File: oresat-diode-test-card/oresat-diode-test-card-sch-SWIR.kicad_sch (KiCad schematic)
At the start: 19 parts, among them Q3 NMOS, Q4 DMP3050LVT-7, U4 TLV6001DCK, U8 NX3L4051-Q100, U9 TLV6001DCK

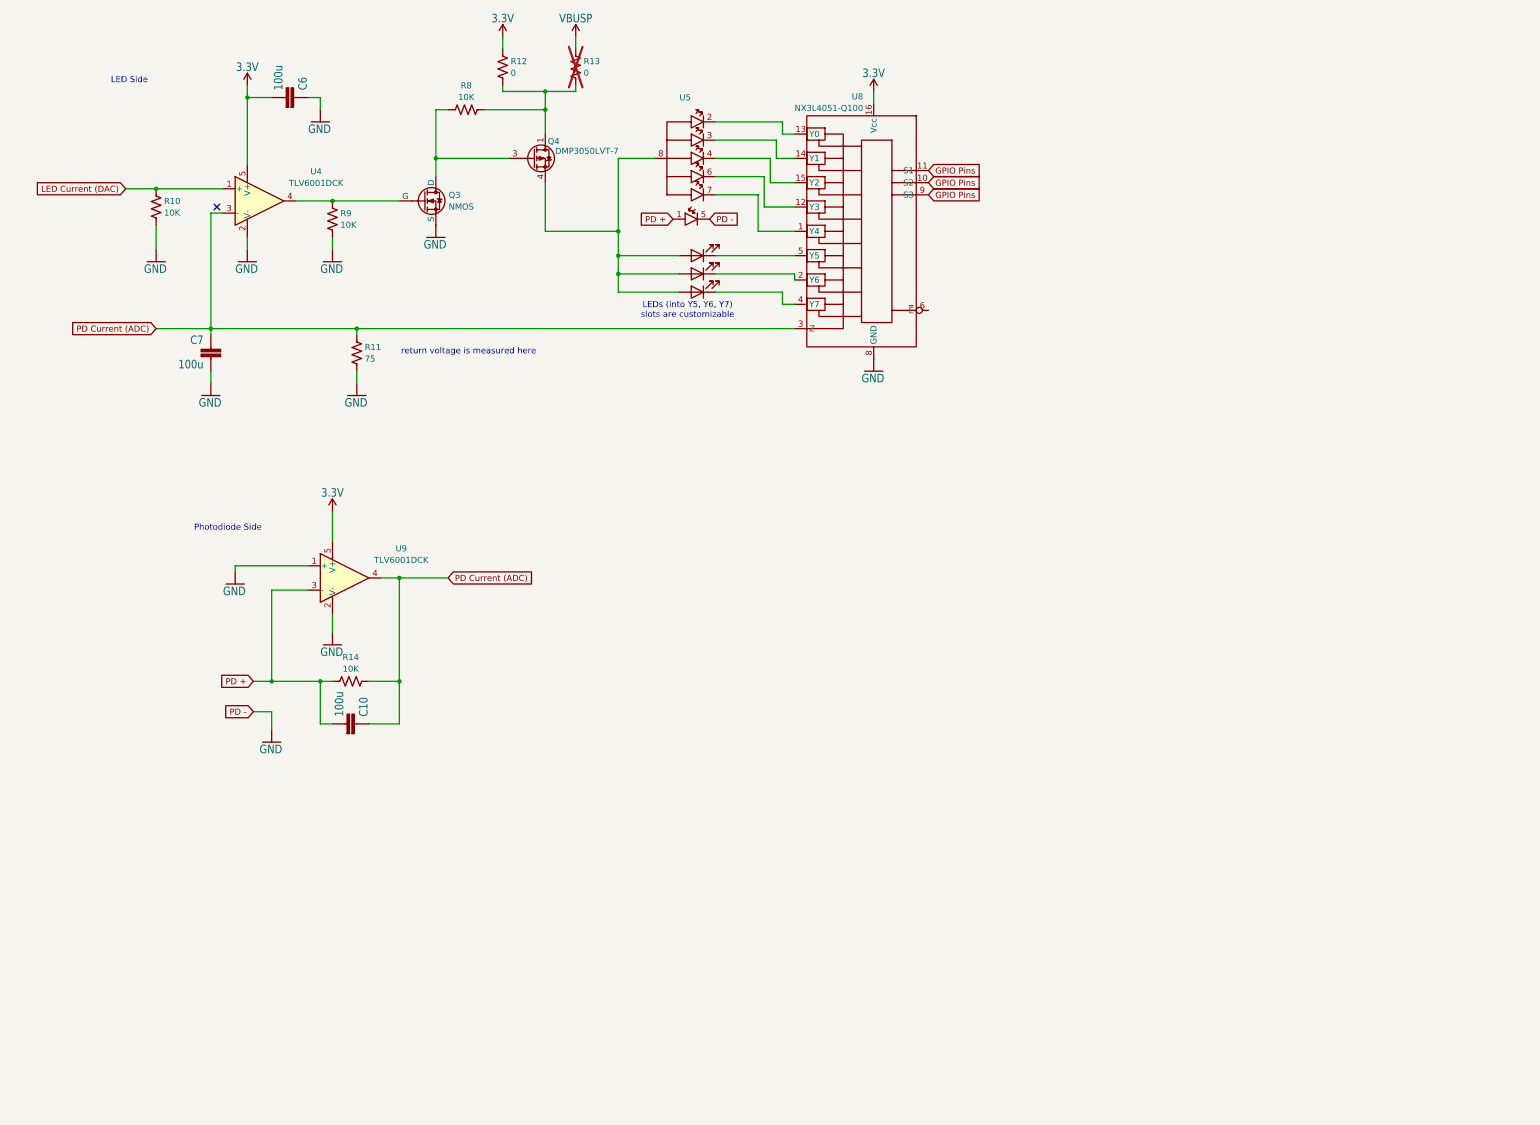
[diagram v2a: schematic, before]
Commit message: Quick design review on schematic; basically ready for layout.
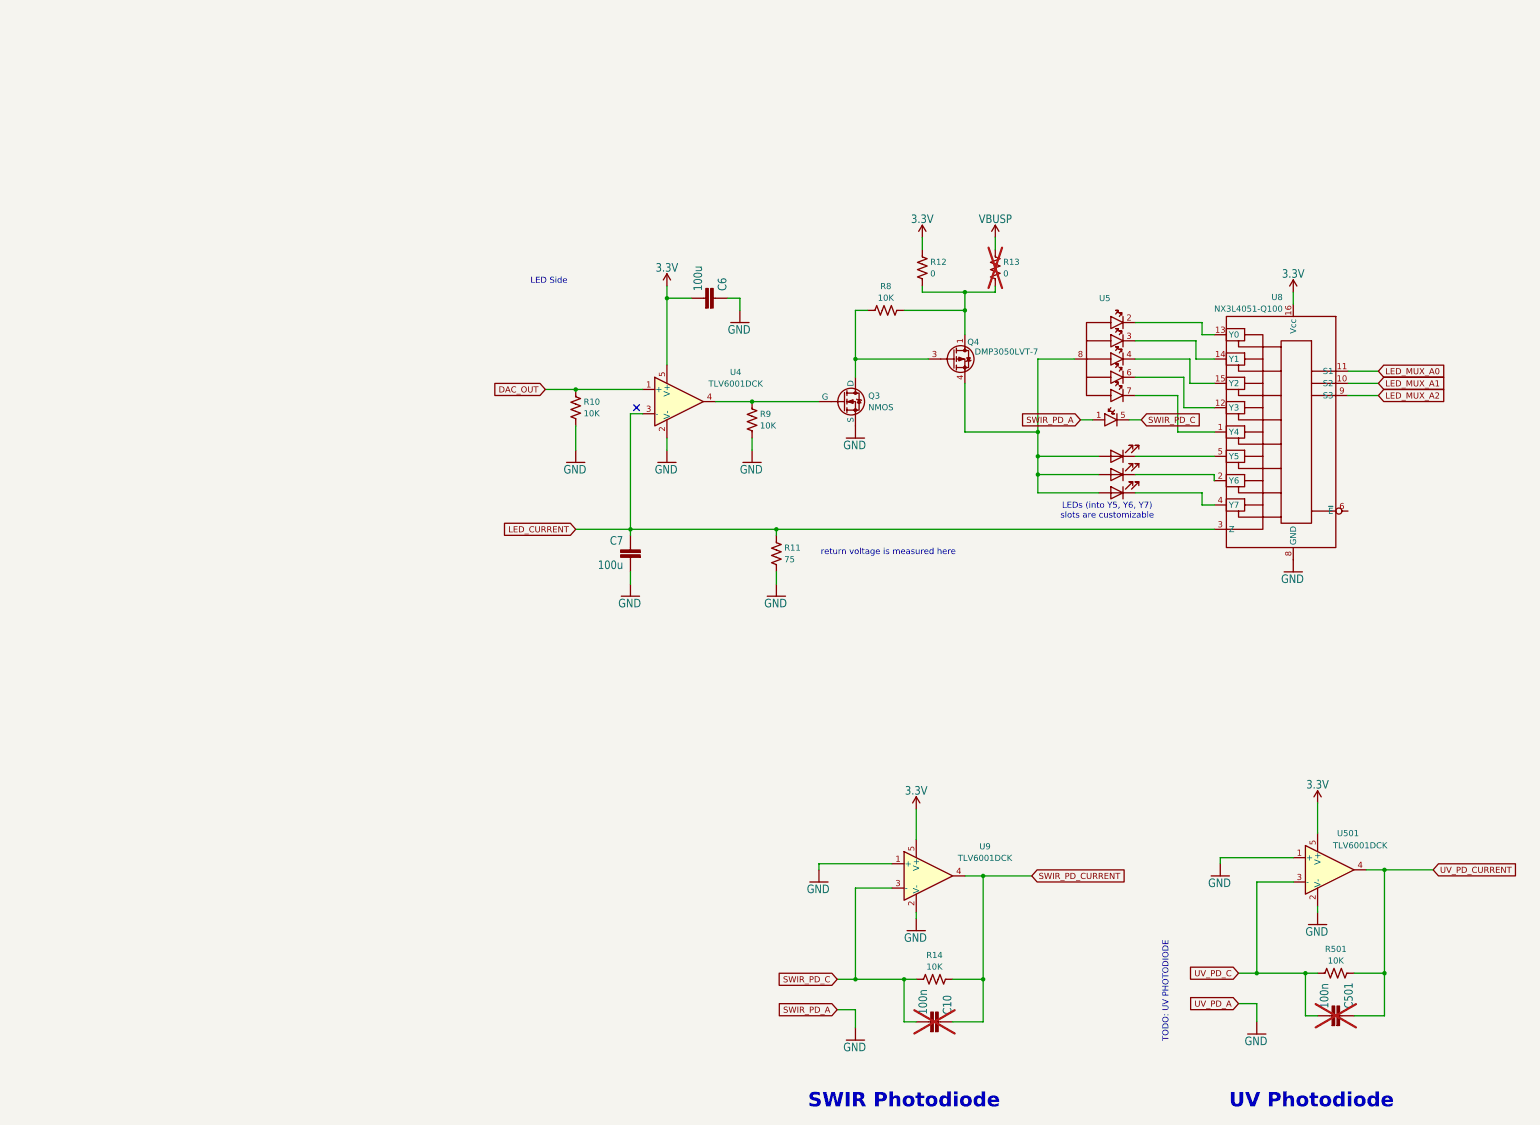
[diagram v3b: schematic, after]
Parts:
- added C501: 100n, oresat-passives:0603-C-NOSILK, symbol oresat-proto-card-eagle-import:C-EU0603-C-NOSILK
- added R501: 10K, symbol Device:R_US
- added U501: TLV6001DCK, Package_TO_SOT_SMD:SOT-353_SC-70-5, symbol Amplifier_Operational:TLV6001DCK
- C10: value 100u -> 100n; now not fitted; now left out of the parts list
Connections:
- net 3.3V: now also U501.5 (V+)
- net GND: now also U5.1 (PD_Anode), U501.1 (+), U501.2 (V-); no longer U5.5 (PD_Cathode)
- removed net GPIO Pins: U8.10 (S2), U8.11 (S1), U8.9 (S3)
- net LED Current (DAC) renamed DAC_OUT
- net PD + renamed SWIR_PD_C
- net SWIR_PD_C: now also U5.5 (PD_Cathode); no longer U5.1 (PD_Anode)
- net PD Current (ADC) renamed LED_CURRENT
- net LED_CURRENT: no longer C10.1, R14.2, U9.4
- new net LED_MUX_A0: U8.11 (S1)
- new net LED_MUX_A1: U8.10 (S2)
- new net LED_MUX_A2: U8.9 (S3)
- new net SWIR_PD_CURRENT: C10.1, R14.2, U9.4
- new net UV_PD_C: C501.2, R501.1, U501.3 (-)
- new net UV_PD_CURRENT: C501.1, R501.2, U501.4
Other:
- note added: "SWIR Photodiode"
- note added: "TODO: UV PHOTODIODE"
- note added: "UV Photodiode"
- note removed: "Photodiode Side"
- title: (none) -> OreSat Diode Test Card
- moved on the sheet: C6, C7, Q3, Q4, R10, R11, R12, R13, R14, R8, R9, U4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

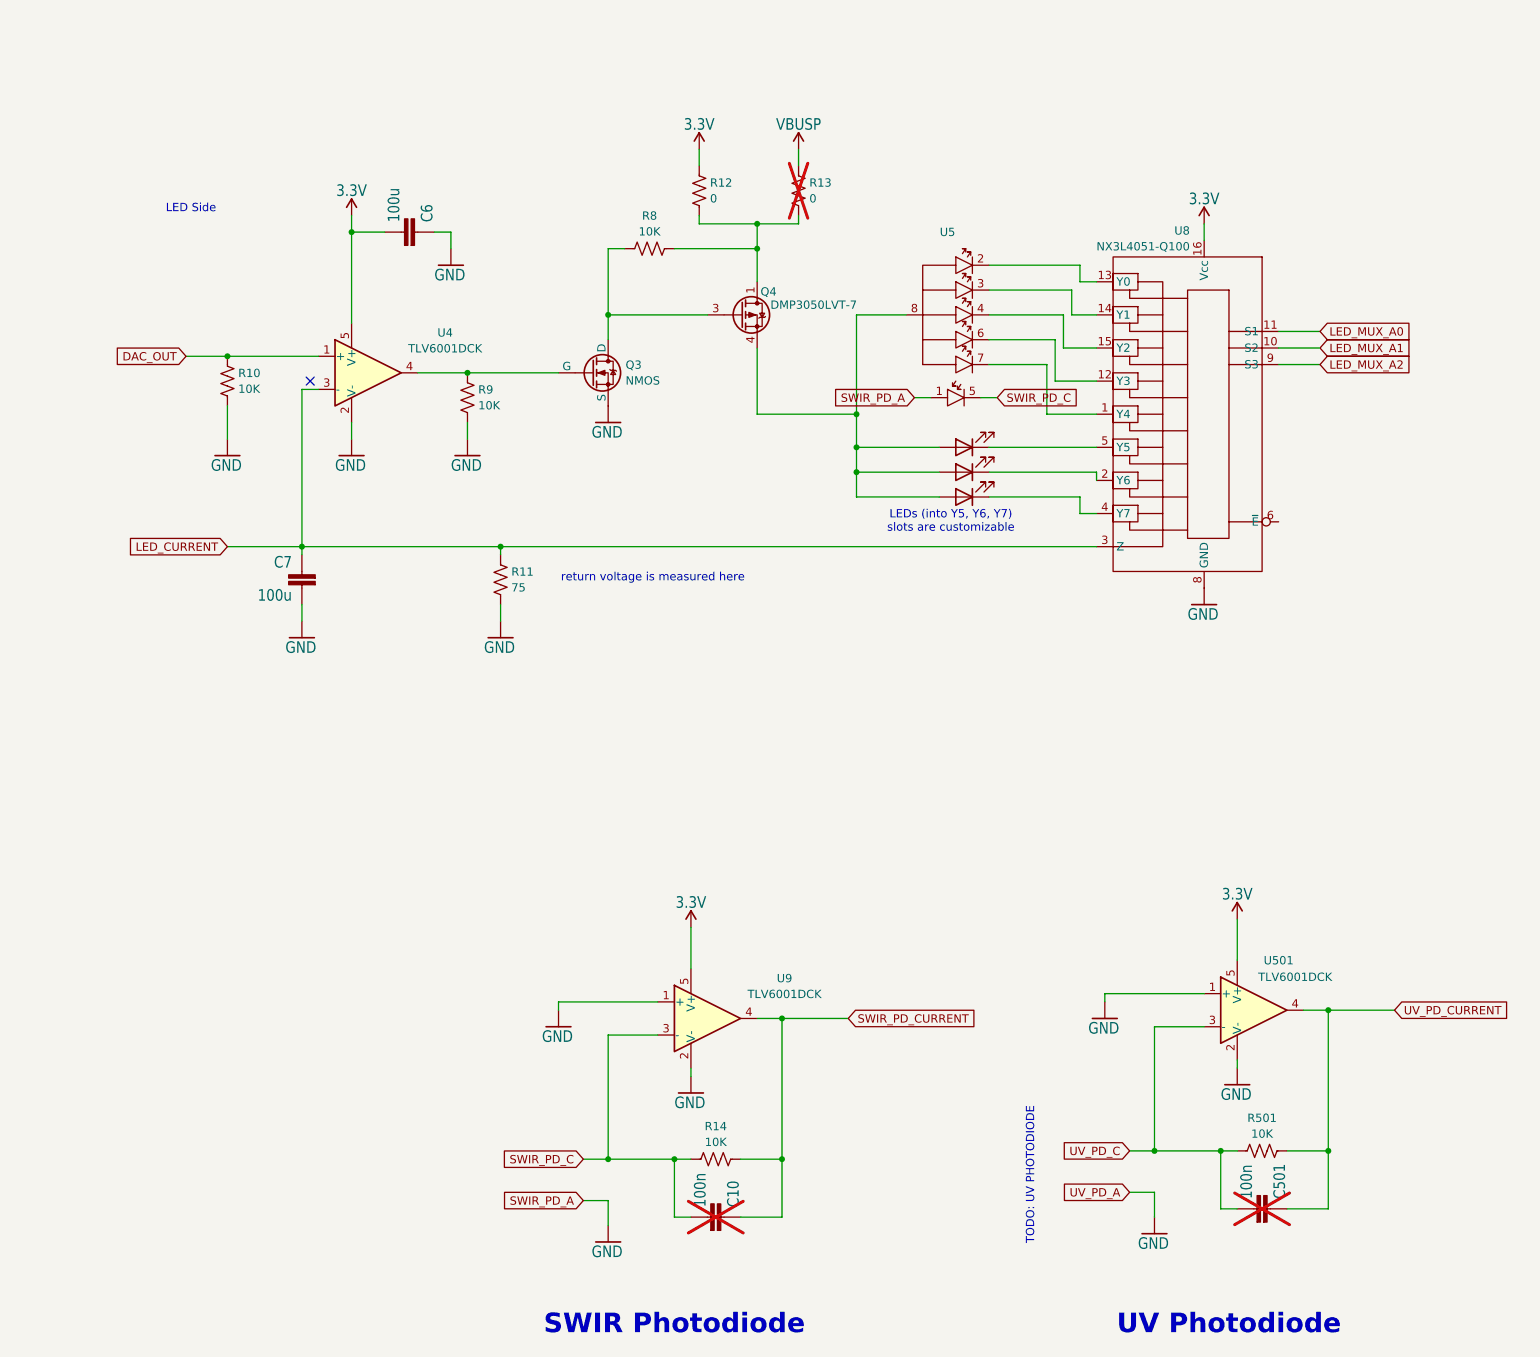
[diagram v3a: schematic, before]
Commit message: Lots of schematic cleanup - replace weird ground and power symbols with more kicad ones, fix values, fix OPD connections and address, update PCB
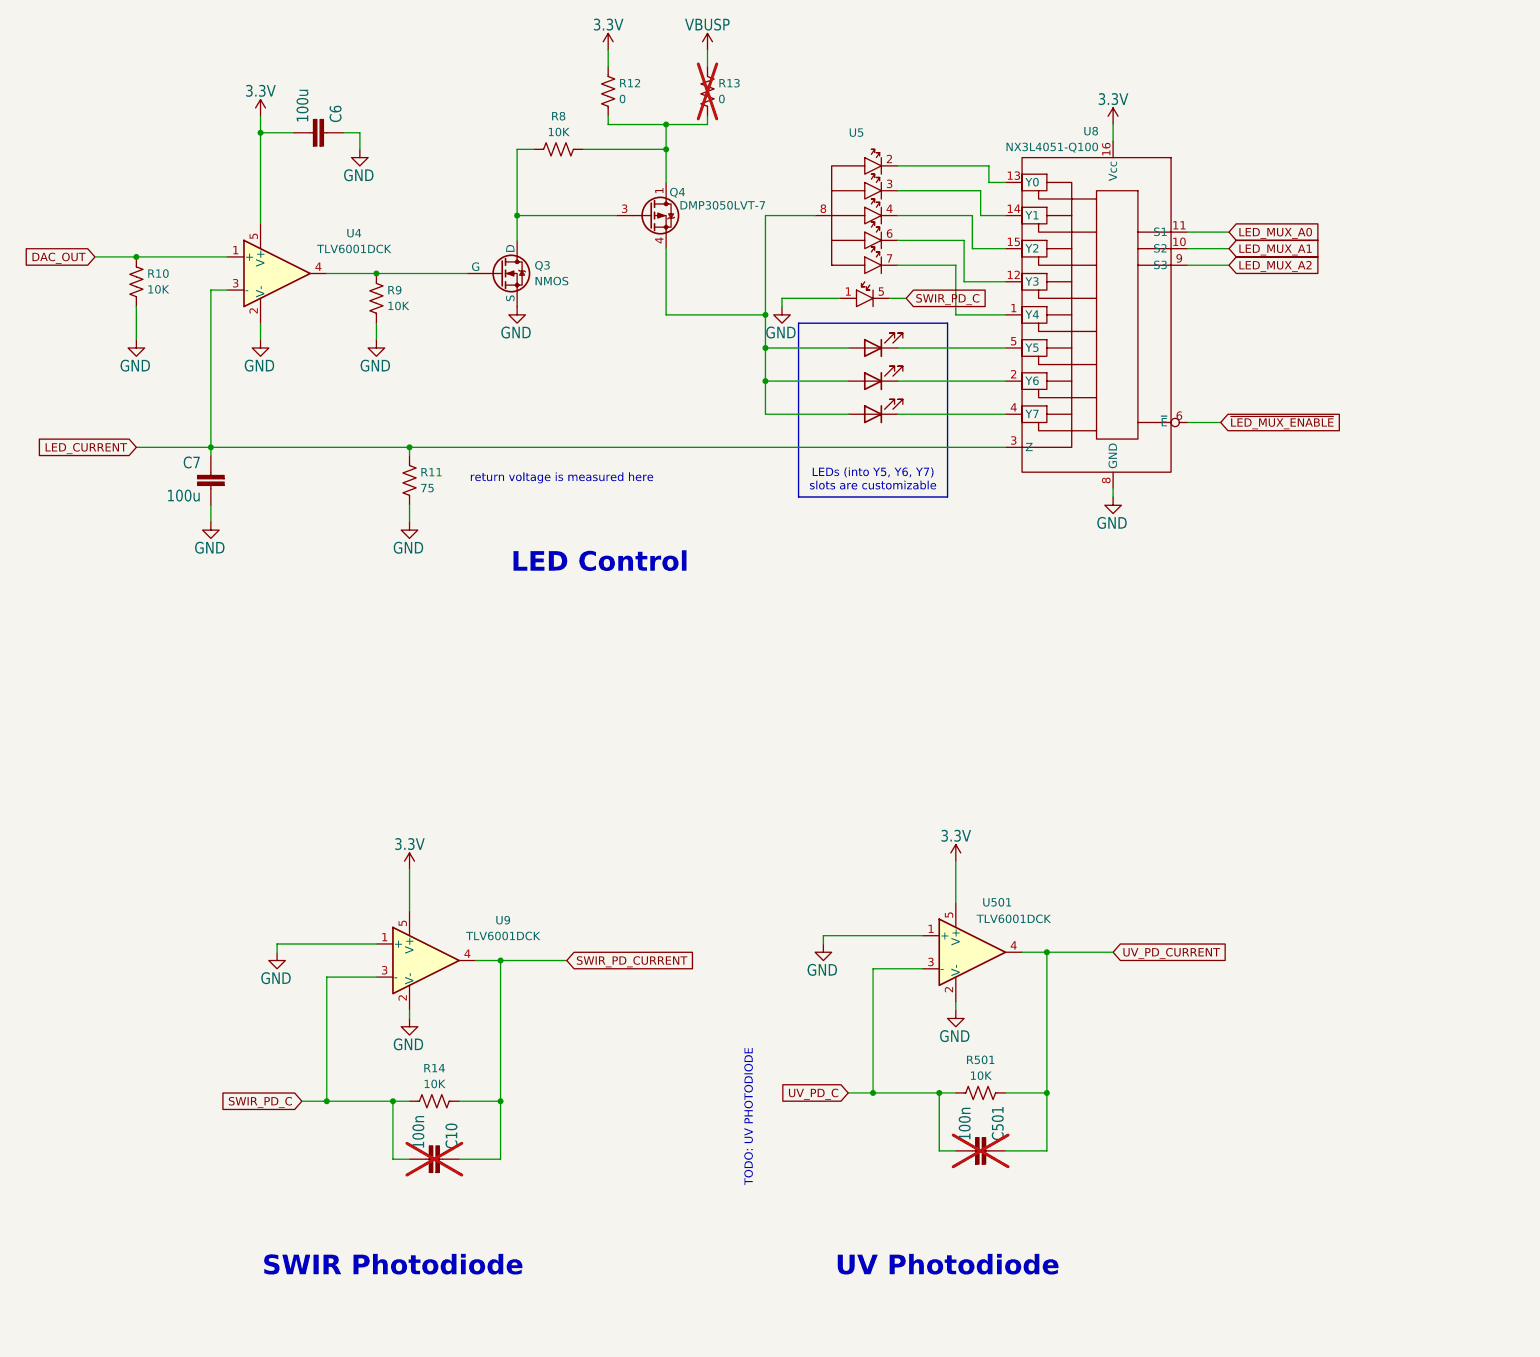
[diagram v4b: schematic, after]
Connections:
- net ~{LED_MUX_ENABLE}: now reaches U8.6 (~{E})
- no-connect marks 1 -> 0
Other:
- note added: "LED Control"
- note removed: "LED Side"
- moved on the sheet: C10, C501, C6, C7, Q3, Q4, R10, R11, R12, R13, R14, R501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
